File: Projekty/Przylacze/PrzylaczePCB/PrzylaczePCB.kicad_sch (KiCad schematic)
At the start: 50 parts, among them J1 Conn_02x20_Odd_Even, J2 USB_B, J3 Conn_01x06, J4 Conn_02x04_Odd_Even, J5 Screw_Terminal_01x06, Q10 BC557, Q11 2N3904, Q3 BC547, Q4 BC557, Q5 2N3904, Q6 BC557, Q8 BC547, Q9 BC557, SW1 SW_Push, U2 ATSAM4S2AA-AU, U6 74AHC1G04, U7 LDL1117S33R, U8 DI78M05UAB, U9 74AHC1G04

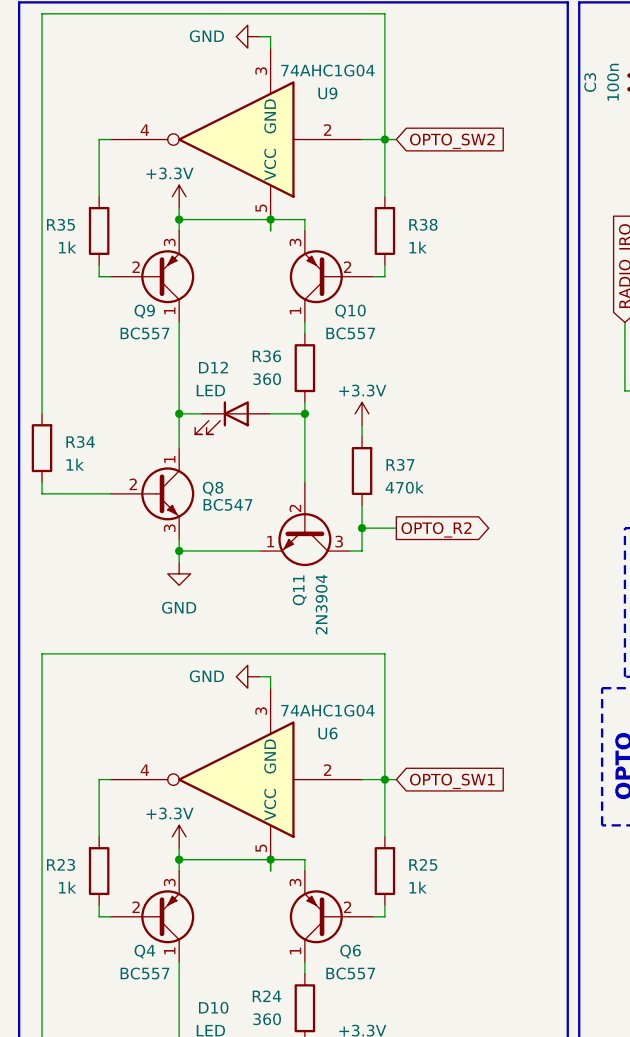
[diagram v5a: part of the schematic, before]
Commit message: Przyłącze - projekt PCB v1.5.1
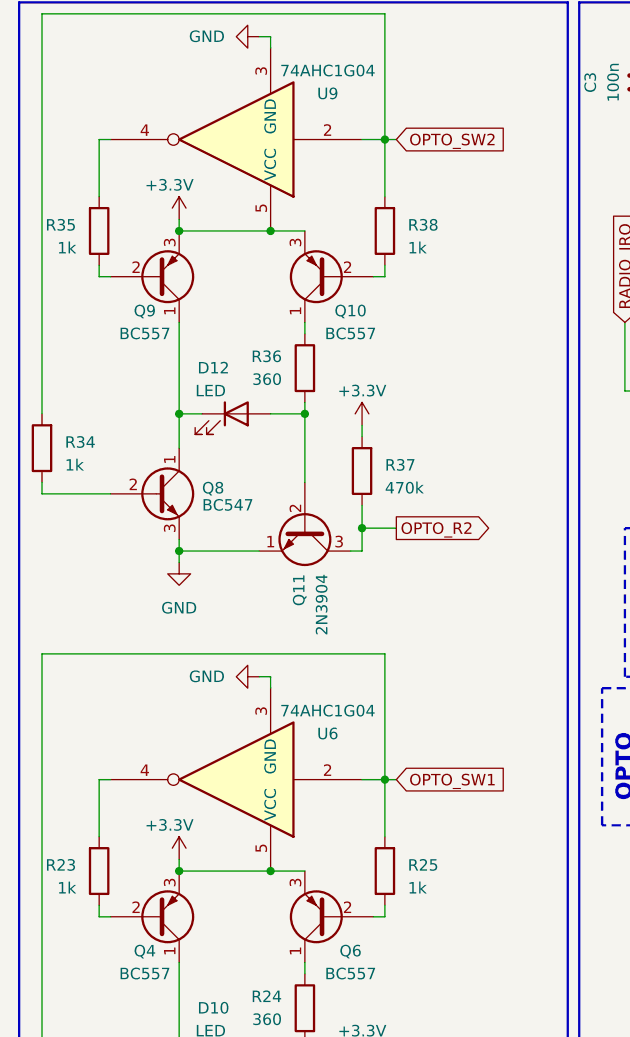
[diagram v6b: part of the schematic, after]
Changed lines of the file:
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@@
   (junction (at 215.9 101.6) (diameter 0) (color 0 0 0 0)
   )
-  (junction (at 43.18 110.49) (diameter 0) (color 0 0 0 0)
-  )
   (junction (at 146.05 20.32) (diameter 0) (color 0 0 0 0)
   )
@@
   (junction (at 33.02 60.96) (diameter 0) (color 0 0 0 0)
   )
-  (junction (at 97.79 48.26) (diameter 0) (color 0 0 0 0)
+  (junction (at 33.02 40.64) (diameter 0) (color 0 0 0 0)
   )
-  (junction (at 43.18 39.37) (diameter 0) (color 0 0 0 0)
+  (junction (at 97.79 48.26) (diameter 0) (color 0 0 0 0)
   )
   (junction (at 95.25 20.32) (diameter 0) (color 0 0 0 0)
@@
   (junction (at 246.38 91.44) (diameter 0) (color 0 0 0 0)
   )
-  (junction (at 33.02 39.37) (diameter 0) (color 0 0 0 0)
-  )
   (junction (at 115.57 48.26) (diameter 0) (color 0 0 0 0)
   )
@@
   (junction (at 115.57 20.32) (diameter 0) (color 0 0 0 0)
   )
+  (junction (at 43.18 111.76) (diameter 0) (color 0 0 0 0)
+  )
   (junction (at 116.84 55.88) (diameter 0) (color 0 0 0 0)
   )
   (junction (at 110.49 27.94) (diameter 0) (color 0 0 0 0)
   )
+  (junction (at 43.18 40.64) (diameter 0) (color 0 0 0 0)
+  )
   (junction (at 105.41 20.32) (diameter 0) (color 0 0 0 0)
   )
@@
   (junction (at 193.04 124.46) (diameter 0) (color 0 0 0 0)
   )
-  (junction (at 33.02 110.49) (diameter 0) (color 0 0 0 0)
-  )
   (junction (at 88.9 162.56) (diameter 0) (color 0 0 0 0)
   )
@@
   (junction (at 267.97 33.02) (diameter 0) (color 0 0 0 0)
   )
+  (junction (at 33.02 111.76) (diameter 0) (color 0 0 0 0)
+  )
   (junction (at 111.76 154.94) (diameter 0) (color 0 0 0 0)
   )
@@
     (stroke (width 0) (type default))
   )
+  (wire (pts (xy 43.18 40.64) (xy 46.99 40.64))
+    (stroke (width 0) (type default))
+  )
   (wire (pts (xy 191.77 45.72) (xy 203.2 45.72))
     (stroke (width 0) (type default))
@@
     (stroke (width 0) (type default))
   )
-  (wire (pts (xy 33.02 110.49) (xy 33.02 111.76))
-    (stroke (width 0) (type default))
-  )
   (wire (pts (xy 264.16 120.65) (xy 261.62 120.65))
     (stroke (width 0) (type default))
@@
     (stroke (width 0) (type default))
   )
-  (wire (pts (xy 46.99 39.37) (xy 46.99 40.64))
-    (stroke (width 0) (type default))
-  )
   (wire (pts (xy 100.33 76.2) (xy 102.87 76.2))
     (stroke (width 0) (type default))
@@
     (stroke (width 0) (type default))
   )
+  (wire (pts (xy 33.02 110.49) (xy 33.02 111.76))
+    (stroke (width 0) (type default))
+  )
   (wire (pts (xy 223.52 73.66) (xy 241.3 73.66))
     (stroke (width 0) (type default))
@@
     (stroke (width 0) (type default))
   )
+  (wire (pts (xy 43.18 111.76) (xy 46.99 111.76))
+    (stroke (width 0) (type default))
+  )
   (wire (pts (xy 46.99 121.92) (xy 46.99 123.19))
     (stroke (width 0) (type default))
@@
     (stroke (width 0) (type default))
   )
-  (wire (pts (xy 33.02 110.49) (xy 43.18 110.49))
+  (wire (pts (xy 33.02 111.76) (xy 43.18 111.76))
     (stroke (width 0) (type default))
   )
@@
     (stroke (width 0) (type default))
   )
-  (wire (pts (xy 43.18 110.49) (xy 46.99 110.49))
-    (stroke (width 0) (type default))
-  )
   (wire (pts (xy 105.41 118.11) (xy 105.41 104.14))
     (stroke (width 0) (type default))
@@
     (stroke (width 0) (type default))
   )
-  (wire (pts (xy 33.02 109.22) (xy 33.02 110.49))
-    (stroke (width 0) (type default))
-  )
   (wire (pts (xy 55.88 30.48) (xy 55.88 36.83))
     (stroke (width 0) (type default))
@@
     (stroke (width 0) (type default))
   )
-  (wire (pts (xy 43.18 39.37) (xy 46.99 39.37))
+  (wire (pts (xy 33.02 40.64) (xy 43.18 40.64))
     (stroke (width 0) (type default))
   )
@@
     (stroke (width 0) (type default))
   )
-  (wire (pts (xy 33.02 38.1) (xy 33.02 39.37))
-    (stroke (width 0) (type default))
-  )
   (wire (pts (xy 109.22 101.6) (xy 118.11 101.6))
     (stroke (width 0) (type default))
@@
     (stroke (width 0) (type default))
   )
-  (wire (pts (xy 43.18 40.64) (xy 43.18 39.37))
-    (stroke (width 0) (type default))
-  )
   (wire (pts (xy 115.57 20.32) (xy 125.73 20.32))
     (stroke (width 0) (type default))
@@
     (stroke (width 0) (type default))
   )
-  (wire (pts (xy 43.18 111.76) (xy 43.18 110.49))
+  (wire (pts (xy 33.02 39.37) (xy 33.02 40.64))
     (stroke (width 0) (type default))
   )
@@
     (stroke (width 0) (type default))
   )
-  (wire (pts (xy 46.99 110.49) (xy 46.99 111.76))
-    (stroke (width 0) (type default))
-  )
   (wire (pts (xy 231.14 58.42) (xy 231.14 63.5))
     (stroke (width 0) (type default))
@@
     (stroke (width 0) (type default))
   )
-  (wire (pts (xy 33.02 39.37) (xy 33.02 40.64))
-    (stroke (width 0) (type default))
-  )
   (wire (pts (xy 55.88 101.6) (xy 57.15 101.6))
     (stroke (width 0) (type default))
   )
-  (wire (pts (xy 33.02 39.37) (xy 43.18 39.37))
-    (stroke (width 0) (type default))
-  )
   (wire (pts (xy 100.33 83.82) (xy 105.41 83.82))
     (stroke (width 0) (type default))
@@
     )
   )
-  (symbol (lib_id "power:+3.3V") (at 33.02 109.22 0) (unit 1)
+  (symbol (lib_id "power:+3.3V") (at 33.02 110.49 0) (unit 1)
     (in_bom yes) (on_board yes) (dnp no)
-    (property "Reference" "#PWR010" (at 33.02 113.03 0)
+    (property "Reference" "#PWR010" (at 33.02 114.3 0)
       (effects (font (size 1.27 1.27)) hide)
     )
-    (property "Value" "+3.3V" (at 29.21 105.41 0)
+    (property "Value" "+3.3V" (at 29.21 106.68 0)
       (effects (font (size 1.27 1.27)) (justify left))
     )
-    (property "Footprint" "" (at 33.02 109.22 0)
+    (property "Footprint" "" (at 33.02 110.49 0)
       (effects (font (size 1.27 1.27)) hide)
     )
-    (property "Datasheet" "" (at 33.02 109.22 0)
+    (property "Datasheet" "" (at 33.02 110.49 0)
       (effects (font (size 1.27 1.27)) hide)
     )
@@
     )
   )
-  (symbol (lib_id "power:+3.3V") (at 33.02 38.1 0) (unit 1)
+  (symbol (lib_id "power:+3.3V") (at 33.02 39.37 0) (unit 1)
     (in_bom yes) (on_board yes) (dnp no)
-    (property "Reference" "#PWR03" (at 33.02 41.91 0)
+    (property "Reference" "#PWR03" (at 33.02 43.18 0)
       (effects (font (size 1.27 1.27)) hide)
     )
-    (property "Value" "+3.3V" (at 29.21 34.29 0)
+    (property "Value" "+3.3V" (at 29.21 35.56 0)
       (effects (font (size 1.27 1.27)) (justify left))
     )
-    (property "Footprint" "" (at 33.02 38.1 0)
+    (property "Footprint" "" (at 33.02 39.37 0)
       (effects (font (size 1.27 1.27)) hide)
     )
-    (property "Datasheet" "" (at 33.02 38.1 0)
+    (property "Datasheet" "" (at 33.02 39.37 0)
       (effects (font (size 1.27 1.27)) hide)
     )

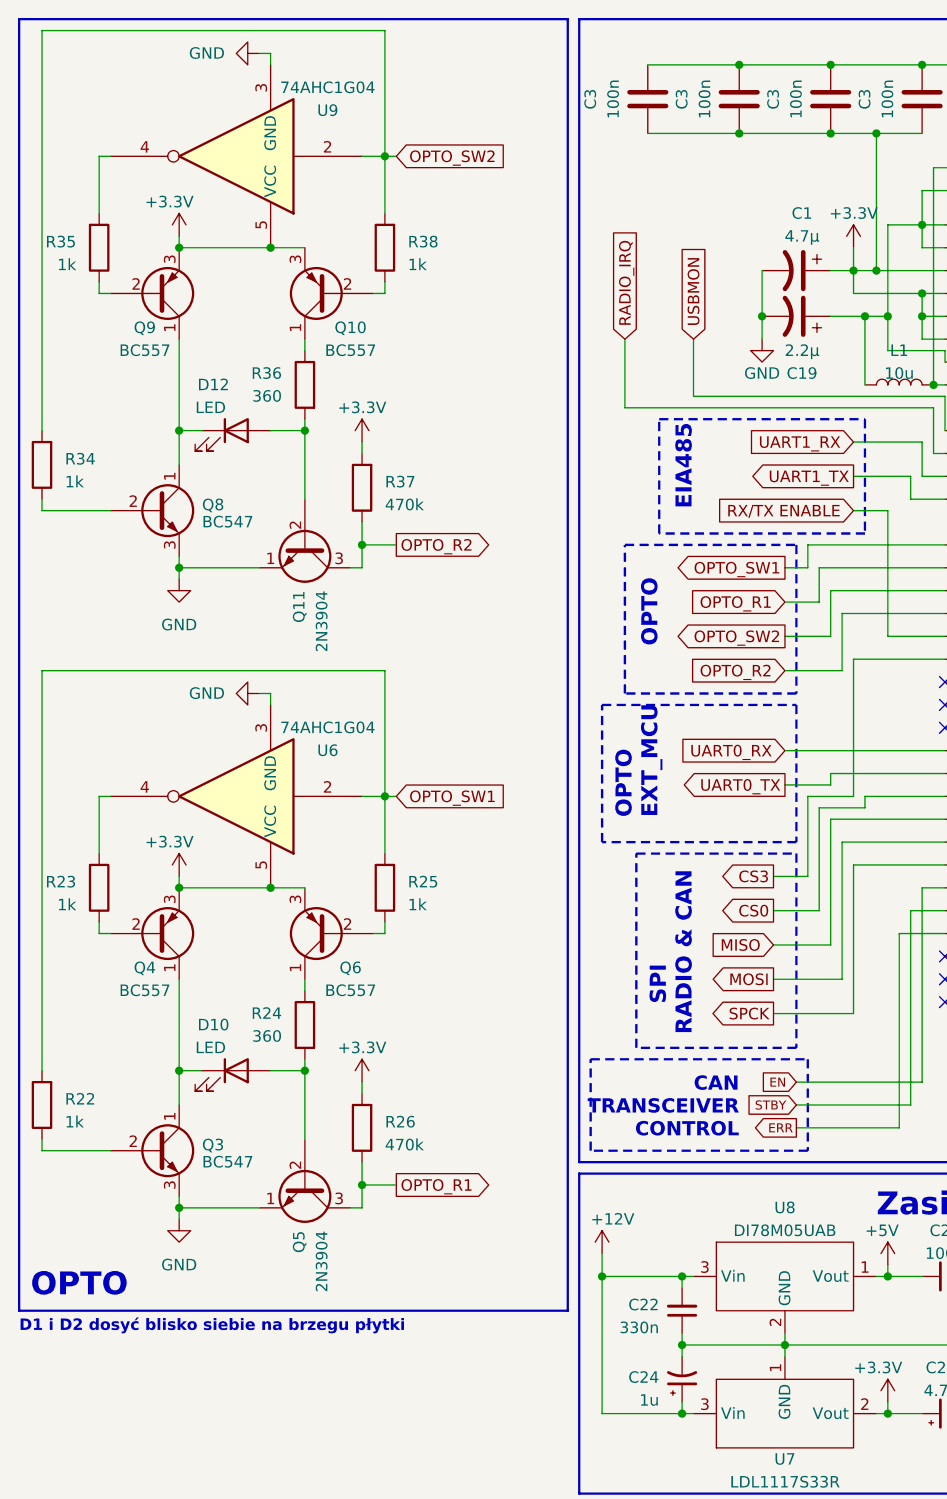
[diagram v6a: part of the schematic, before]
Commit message: Przyłącze - schemat elektryczny v1.4
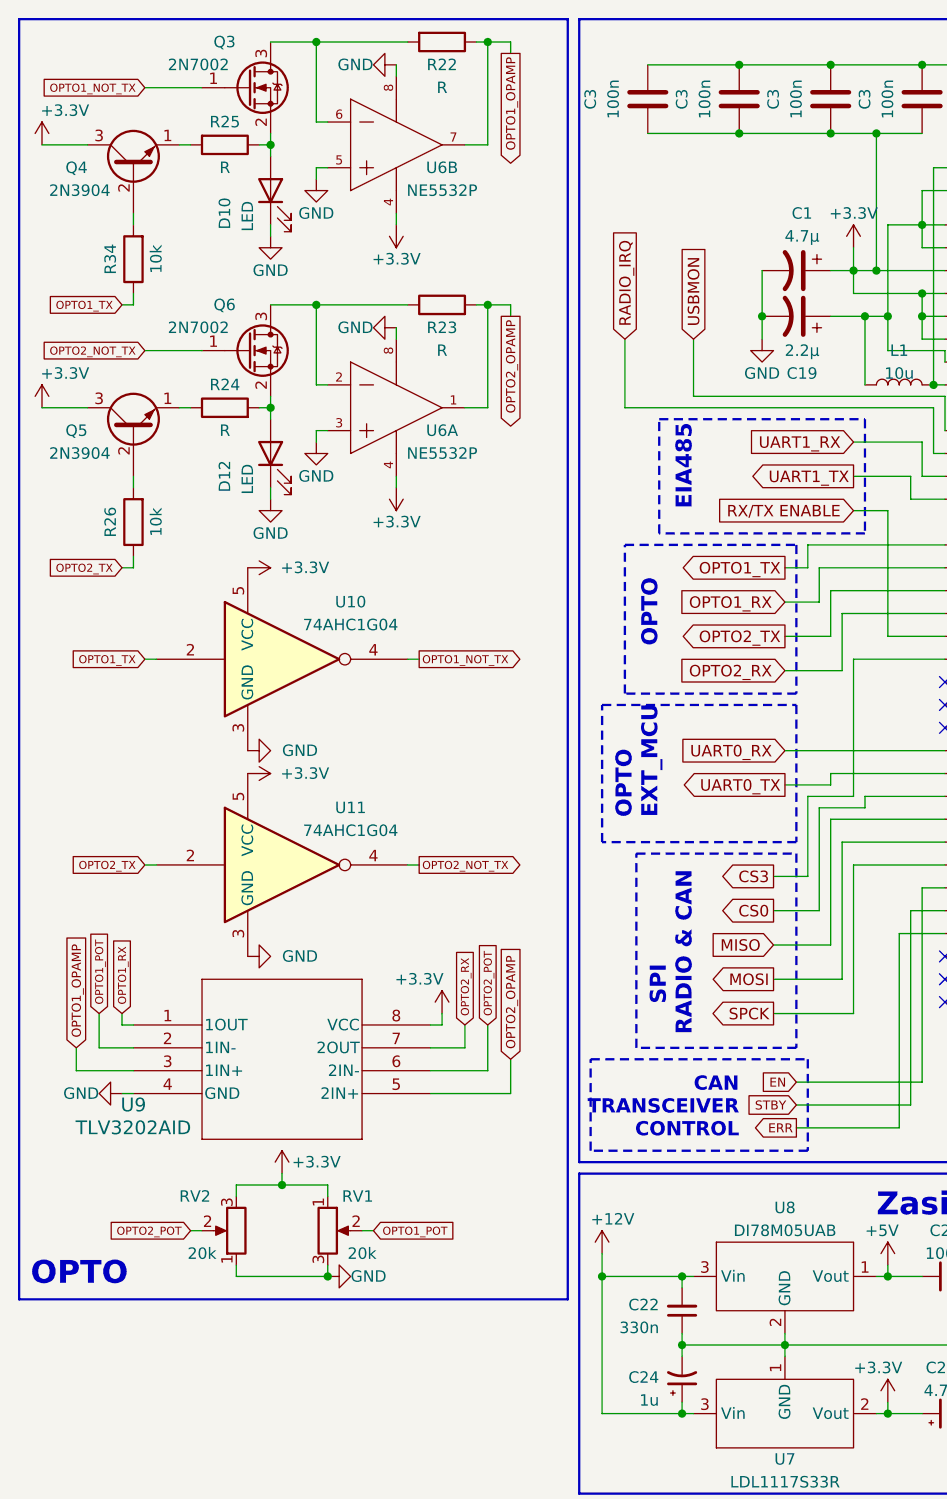
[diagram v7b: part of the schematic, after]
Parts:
- removed Q10, Q4, Q6, Q9: BC557, Package_TO_SOT_THT:TO-92L, symbol Transistor_BJT:BC557
- removed Q11: 2N3904, Package_TO_SOT_THT:TO-92L, symbol Transistor_BJT:2N3904
- removed Q3, Q8: BC547, Package_TO_SOT_THT:TO-92L, symbol Transistor_BJT:BC547
- removed R35, R38: 1k, Resistor_THT:R_Axial_DIN0207_L6.3mm_D2.5mm_P7.62mm_Horizontal, symbol Device:R
- removed R36: 360, Resistor_THT:R_Axial_DIN0207_L6.3mm_D2.5mm_P7.62mm_Horizontal, symbol Device:R
- removed R37: 470k, Resistor_THT:R_Axial_DIN0207_L6.3mm_D2.5mm_P7.62mm_Horizontal, symbol Device:R
- removed U6, U9: 74AHC1G04, PrzylaczeFootprintLibrary:Nexperia-SOT753-10_2018-0-0, symbol 74xGxx:74AHC1G04
- added Q3, Q6: 2N7002, Package_TO_SOT_SMD:SOT-23, symbol Transistor_FET:2N7002
- added Q4: 2N3904, Package_TO_SOT_THT:TO-92_Inline, symbol Transistor_BJT:2N3904
- added RV1, RV2: 20k, symbol Device:R_Potentiometer
- added U10, U11: 74AHC1G04, symbol 74xGxx:74AHC1G04
- added U6: NE5532P, PrzylaczeFootprintLibrary:Texas_Instruments-NE5532P, symbol PrzylaczePCBLib:NE5532P
- added U9: TLV3202AID, D8_TEX, symbol PrzylaczePCBLib:TLV3202AID
- Q5: footprint Package_TO_SOT_THT:TO-92L -> Package_TO_SOT_THT:TO-92_Inline
- R22, R23, R25: value 1k -> R; footprint Resistor_THT:R_Axial_DIN0207_L6.3mm_D2.5mm_P7.62mm_Horizontal -> (none)
- R24: value 360 -> R; footprint Resistor_THT:R_Axial_DIN0207_L6.3mm_D2.5mm_P7.62mm_Horizontal -> (none)
- R26: value 470k -> 10k; footprint Resistor_THT:R_Axial_DIN0207_L6.3mm_D2.5mm_P7.62mm_Horizontal -> (none)
- R34: value 1k -> 10k; footprint Resistor_THT:R_Axial_DIN0207_L6.3mm_D2.5mm_P7.62mm_Horizontal -> (none)
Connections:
- net +3.3V: now also Q5.3 (C), Q4.3 (C), RV1.1, RV2.3, U10.5 (VCC), U11.5 (VCC), U6.4 (VCC-), U6.4 (VCC-), U9.8 (VCC); no longer R26.2
- net GND: now also D10.1 (K), D12.1 (K), RV1.3, RV2.1, U10.3 (GND), U11.3 (GND), U6.3 (IN1+), U6.5 (IN2+), U6.8 (VCC+), U6.8 (VCC+), U9.4 (GND); no longer Q5.1 (E)
- net OPTO_R1: no longer Q5.3 (C), R26.1, U2.35 (PA1/PGMEN1)
- net OPTO_R2: no longer U2.31 (PA3)
- net OPTO_SW1: no longer R22.2, R25.2, U2.36 (PA0/PGMEN0)
- net OPTO_SW2: no longer R34.2, U2.32 (PA2/PGMEN2)
- net at D12.2 (A): now also R24.2, Q6.2 (S)
- net at R25.1: now also D10.2 (A), Q3.2 (S)
- net at R24.1: now also Q5.1 (E)
- net at R23.1: now also Q6.3 (D), U6.2 (IN1-)
- net OPTO2_OPAMP: now reaches R23.2
- net OPTO2_OPAMP: now also U6.1 (OUT1), U9.5 (2IN+)
- net OPTO1_OPAMP: now reaches R22.1
- net OPTO1_OPAMP: now also U6.7 (OUT2), U9.3 (1IN+)
- net OPTO1_TX: now reaches R34.1
- net OPTO1_TX: now also U2.36 (PA0/PGMEN0), U10.2
- new net: Q5.2 (B), R26.2
- new net: Q4.1 (E), R25.2
- new net: Q3.3 (D), R22.2, U6.6 (IN2-)
- new net: Q4.2 (B), R34.2
- new net OPTO1_NOT_TX: Q3.1 (G), U10.4
- new net OPTO1_POT: RV1.2, U9.2 (1IN-)
- new net OPTO1_RX: U2.35 (PA1/PGMEN1), U9.1 (1OUT)
- new net OPTO2_NOT_TX: Q6.1 (G), U11.4
- new net OPTO2_POT: RV2.2, U9.6 (2IN-)
- new net OPTO2_RX: U2.31 (PA3), U9.7 (2OUT)
- new net OPTO2_TX: R26.1, U11.2, U2.32 (PA2/PGMEN2)
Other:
- note removed: "D1 i D2 dosyć blisko siebie na brzegu płytki"
- moved on the sheet: D10, D12

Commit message: Przyłącze - schemat elektryczny v1.4.1
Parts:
- R22, R23, R24, R25, R26, R34: footprint (none) -> Resistor_THT:R_Axial_DIN0207_L6.3mm_D2.5mm_P10.16mm_Horizontal
- RV1, RV2: footprint (none) -> Potentiometer_THT:Potentiometer_Bourns_3006P_Horizontal; Field4 (none) -> https://www.tme.eu/pl/details/3006p-1-203lf
- U10, U11: footprint (none) -> PrzylaczeFootprintLibrary:Nexperia-SOT753-10_2018-0-0
- U9: footprint D8_TEX -> PrzylaczeFootprintLibrary:TLV3202AID
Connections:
- net OPTO_R1 is gone; now on net OPTO1_RX: J1.4 (Pin_4)
- net OPTO_R2 is gone; now on net OPTO2_RX: J1.2 (Pin_2)
- net OPTO_SW1 is gone; now on net OPTO1_TX: J1.3 (Pin_3)
- net OPTO_SW2 is gone; now on net OPTO2_TX: J1.1 (Pin_1)
